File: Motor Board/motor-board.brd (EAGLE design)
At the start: 60 x 22 mm, 11 parts

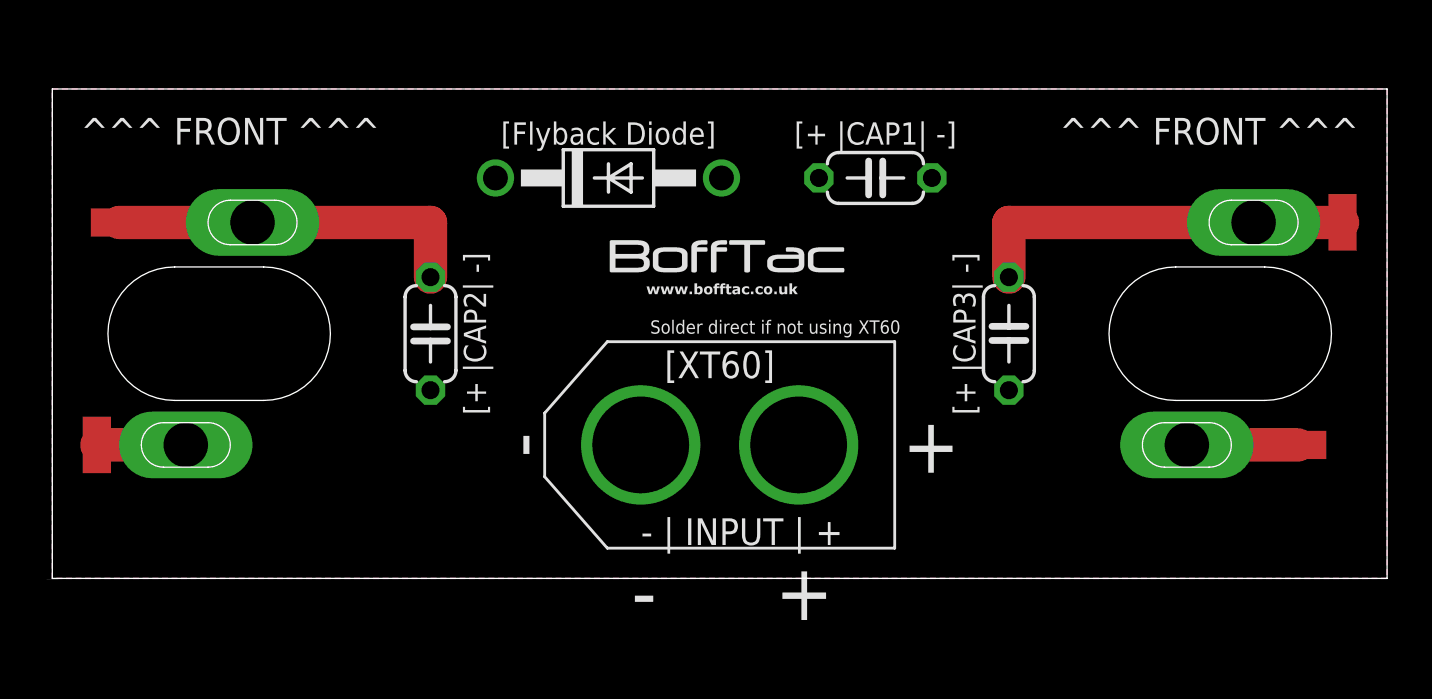
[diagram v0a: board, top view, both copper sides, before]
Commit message: Board Update
Redefined 130 motor can and updated board to add solder pads if not using XT60 connectors
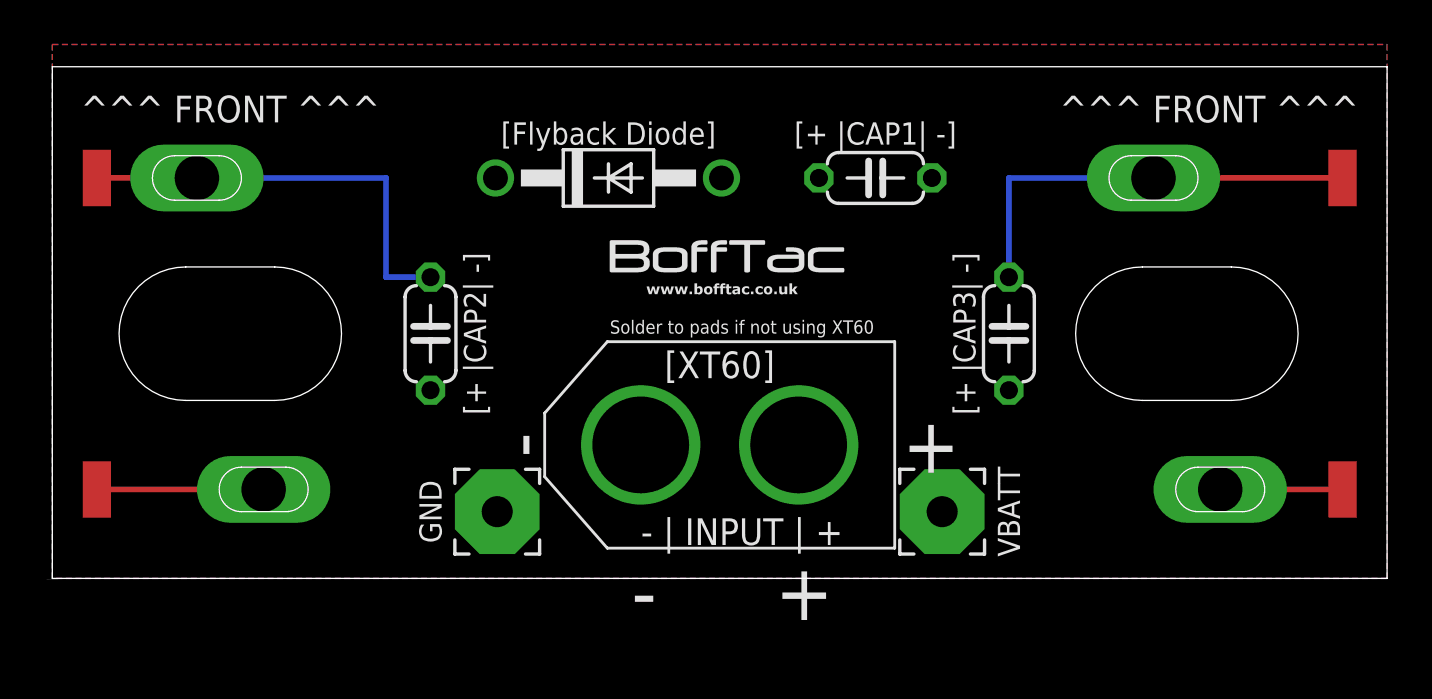
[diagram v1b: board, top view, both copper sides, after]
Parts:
- removed BOTTOM-MOTOR, TOP-MOTOR: (no value), 130-can:130-MOTOR-CAN
- removed PAD2, PAD3: (no value), wirepad:SMD1,27-2,54
- added BOTTOM-CAN, TOP-CAN: (no value), wirepad:SMD1,27-2,54
- added PAD-GND, PAD-VBATT: (no value), wirepad:3,81/1,4
- added U$1, U$2: 130-CAN-DEVICE130-MOTOR-CAN, 130-can:130-MOTOR-CAN
- moved PAD1 12.0 mm to (2.00, 18.0)
- moved PAD4 2.00 mm to (58.0, 18.0)
- turned C3 to 90 degrees
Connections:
- net GND: now also C1.2, C3.2, PAD-GND.1, PAD1.1, U$1.MOTOR-VE, U$2.MOTOR-VE; no longer BOTTOM-MOTOR.MOTOR-VE, C1.1, C3.1, PAD2.1, TOP-MOTOR.MOTOR-VE
- net VBATT: now also BOTTOM-CAN.1, C1.1, C3.1, PAD-VBATT.1, TOP-CAN.1, U$1.MOTOR+VE, U$2.MOTOR+VE; no longer BOTTOM-MOTOR.MOTOR+VE, C1.2, C3.2, PAD1.1, PAD3.1, TOP-MOTOR.MOTOR+VE
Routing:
- net GND: track 33.9 -> 38.9 mm
- net VBATT: track 9.00 -> 13.0 mm
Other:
- board size 60 x 22 mm -> 60 x 23 mm
- board text added: "GND"
- board text added: "Solder to pads if not using XT60"
- board text added: "VBATT"
- board text removed: "Solder direct if not using XT60"
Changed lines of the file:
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@@
 <plain>
 <wire x1="0" y1="0" x2="60" y2="0" width="0" layer="20"/>
-<wire x1="60" y1="0" x2="60" y2="22" width="0" layer="20"/>
-<wire x1="0" y1="22" x2="0" y2="0" width="0" layer="20"/>
-<wire x1="0" y1="22" x2="60" y2="22" width="0" layer="20"/>
+<wire x1="60" y1="0" x2="60" y2="23" width="0" layer="20"/>
+<wire x1="0" y1="23" x2="0" y2="0" width="0" layer="20"/>
+<wire x1="0" y1="23" x2="60" y2="23" width="0" layer="20"/>
 <text x="19" y="11" size="1" layer="25" ratio="12" rot="R90" align="center">[+ |CAP2| -]</text>
 <text x="25" y="19.5" size="1" layer="25" ratio="12" align="bottom-center">[Flyback Diode]</text>
 <text x="37" y="20" size="1" layer="25" ratio="12" rot="R180" align="center">[+ |CAP1| -]</text>
 <text x="41" y="11" size="1" layer="25" ratio="12" rot="R270" align="center">[+ |CAP3| -]</text>
-<text x="8" y="19.5" size="1.2" layer="25" ratio="12" align="bottom-center">^^^ FRONT ^^^</text>
-<text x="52" y="19.5" size="1.2" layer="25" ratio="12" align="bottom-center">^^^ FRONT ^^^</text>
+<text x="8" y="20.5" size="1.2" layer="25" ratio="12" align="bottom-center">^^^ FRONT ^^^</text>
+<text x="52" y="20.5" size="1.2" layer="25" ratio="12" align="bottom-center">^^^ FRONT ^^^</text>
 <text x="31" y="1.5" size="1.2" layer="25" ratio="12" align="bottom-center">- | INPUT | +</text>
-<text x="32.5" y="11" size="0.6" layer="25" ratio="12" align="bottom-center">Solder direct if not using XT60</text>
+<text x="31" y="11" size="0.6" layer="25" ratio="12" align="bottom-center">Solder to pads if not using XT60</text>
 <text x="30" y="9" size="1.2" layer="25" ratio="12" align="bottom-center">[XT60]</text>
 <text x="39.5" y="6" size="2.5" layer="25" ratio="12" align="center">+</text>
@@
 <rectangle x1="30.465" y1="15.195" x2="32.005" y2="15.205" layer="25"/>
 <text x="0" y="-0.05" size="0.02" layer="25" font="vector" ratio="12" align="bottom-center">Y:/BoffTac/Logo/monologo-w-address.bmp</text>
+<text x="17" y="3" size="1" layer="25" ratio="12" rot="R90" align="center">GND</text>
+<text x="43" y="3" size="1" layer="25" ratio="12" rot="R90" align="center">VBATT</text>
 </plain>
 <attributes>
@@
 <attribute name="VALUE" x="37.8675" y="10.94" size="1.27" layer="27" align="bottom-right"/>
 </element>
-<element name="TOP-MOTOR" library="130-can" package="130-MOTOR-CAN" value="" x="8" y="11" rot="R90"/>
-<element name="BOTTOM-MOTOR" library="130-can" package="130-MOTOR-CAN" value="" x="53" y="11" smashed="yes" rot="R90"/>
 <element name="C1" library="resistor" package="C050-024X044" value="" x="37" y="18" smashed="yes">
 <attribute name="VALUE" x="34.841" y="15.333" size="1.27" layer="27" ratio="10"/>
@@
 <attribute name="VALUE" x="45.667" y="8.841" size="1.27" layer="27" ratio="10" rot="R90"/>
 </element>
-<element name="C3" library="resistor" package="C050-024X044" value="" x="17" y="11" smashed="yes" rot="R270">
-<attribute name="VALUE" x="14.333" y="13.159" size="1.27" layer="27" ratio="10" rot="R270"/>
+<element name="C3" library="resistor" package="C050-024X044" value="" x="17" y="11" smashed="yes" rot="R90">
+<attribute name="VALUE" x="19.667" y="8.841" size="1.27" layer="27" ratio="10" rot="R90"/>
 </element>
-<element name="PAD1" library="wirepad" package="SMD1,27-2,54" value="" x="2" y="6" smashed="yes">
-<attribute name="VALUE" x="2" y="6" size="0.0254" layer="27"/>
+<element name="PAD1" library="wirepad" package="SMD1,27-2,54" value="" x="2" y="18" smashed="yes">
+<attribute name="VALUE" x="2" y="18" size="0.0254" layer="27"/>
 </element>
-<element name="PAD2" library="wirepad" package="SMD1,27-2,54" value="" x="3" y="16" smashed="yes" rot="R270">
-<attribute name="VALUE" x="3" y="16" size="0.0254" layer="27" rot="R270"/>
+<element name="TOP-CAN" library="wirepad" package="SMD1,27-2,54" value="" x="2" y="4" smashed="yes">
+<attribute name="VALUE" x="2" y="4" size="0.0254" layer="27"/>
 </element>
-<element name="PAD3" library="wirepad" package="SMD1,27-2,54" value="" x="56" y="6" smashed="yes" rot="R90">
-<attribute name="VALUE" x="56" y="6" size="0.0254" layer="27" rot="R90"/>
+<element name="BOTTOM-CAN" library="wirepad" package="SMD1,27-2,54" value="" x="58" y="4" smashed="yes" rot="R180">
+<attribute name="VALUE" x="58" y="4" size="0.0254" layer="27" rot="R180"/>
 </element>
-<element name="PAD4" library="wirepad" package="SMD1,27-2,54" value="" x="58" y="16" smashed="yes" rot="R180">
-<attribute name="VALUE" x="58" y="16" size="0.0254" layer="27" rot="R180"/>
+<element name="PAD4" library="wirepad" package="SMD1,27-2,54" value="" x="58" y="18" smashed="yes" rot="R180">
+<attribute name="VALUE" x="58" y="18" size="0.0254" layer="27" rot="R180"/>
+</element>
+<element name="U$1" library="130-can" package="130-MOTOR-CAN" value="130-CAN-DEVICE130-MOTOR-CAN" x="7.5" y="11" rot="MR90"/>
+<element name="U$2" library="130-can" package="130-MOTOR-CAN" value="130-CAN-DEVICE130-MOTOR-CAN" x="50.5" y="11" rot="MR90"/>
+<element name="PAD-GND" library="wirepad" package="3,81/1,4" value="" x="20" y="3" smashed="yes">
+<attribute name="VALUE" x="20" y="4.2" size="0.0254" layer="27"/>
+</element>
+<element name="PAD-VBATT" library="wirepad" package="3,81/1,4" value="" x="40" y="3" smashed="yes">
+<attribute name="VALUE" x="40" y="4.2" size="0.0254" layer="27"/>
 </element>
 </elements>
@@
 <signal name="GND">
 <polygon width="0.254" layer="16" isolate="0.3048">
-<vertex x="0" y="22"/>
-<vertex x="60" y="22"/>
+<vertex x="0" y="24"/>
+<vertex x="60" y="24"/>
 <vertex x="60" y="0"/>
 <vertex x="0" y="0"/>
 </polygon>
-<contactref element="TOP-MOTOR" pad="MOTOR-VE"/>
-<contactref element="BOTTOM-MOTOR" pad="MOTOR-VE"/>
+<contactref element="U$2" pad="MOTOR-VE"/>
 <contactref element="J1" pad="-"/>
+<contactref element="U$1" pad="MOTOR-VE"/>
+<contactref element="C1" pad="2"/>
+<contactref element="C2" pad="2"/>
+<contactref element="C3" pad="2"/>
+<contactref element="PAD4" pad="1"/>
+<contactref element="PAD1" pad="1"/>
+<wire x1="49.5" y1="18" x2="43" y2="18" width="0.254" layer="16"/>
+<wire x1="43" y1="18" x2="43" y2="13.54" width="0.254" layer="16"/>
+<wire x1="58" y1="18" x2="49.5" y2="18" width="0.254" layer="1"/>
+<wire x1="17" y1="13.54" x2="15" y2="13.54" width="0.254" layer="16"/>
+<wire x1="15" y1="13.54" x2="15" y2="18" width="0.254" layer="16"/>
+<wire x1="15" y1="18" x2="6.5" y2="18" width="0.254" layer="16"/>
 <contactref element="D1" pad="A"/>
-<contactref element="C1" pad="1"/>
-<contactref element="C2" pad="2"/>
-<contactref element="C3" pad="1"/>
-<contactref element="PAD2" pad="1"/>
-<contactref element="PAD4" pad="1"/>
-<wire x1="54" y1="16" x2="43" y2="16" width="1.5" layer="1"/>
-<wire x1="43" y1="16" x2="43" y2="13.54" width="1.5" layer="1"/>
-<wire x1="58" y1="16" x2="54" y2="16" width="1.5" layer="1"/>
-<wire x1="3" y1="16" x2="9" y2="16" width="1.5" layer="1"/>
-<wire x1="17" y1="13.54" x2="17" y2="16" width="1.5" layer="1"/>
-<wire x1="17" y1="16" x2="9" y2="16" width="1.5" layer="1"/>
+<wire x1="2" y1="18" x2="6.5" y2="18" width="0.254" layer="1"/>
+<contactref element="PAD-GND" pad="1"/>
 </signal>
 <signal name="VBATT">
 <polygon width="0.254" layer="1" isolate="0.3048">
-<vertex x="0" y="22"/>
-<vertex x="60" y="22"/>
+<vertex x="0" y="24"/>
+<vertex x="60" y="24"/>
 <vertex x="60" y="0"/>
 <vertex x="0" y="0"/>
 </polygon>
-<contactref element="BOTTOM-MOTOR" pad="MOTOR+VE"/>
-<contactref element="TOP-MOTOR" pad="MOTOR+VE"/>
 <contactref element="J1" pad="+"/>
+<contactref element="U$1" pad="MOTOR+VE"/>
+<contactref element="U$2" pad="MOTOR+VE"/>
+<contactref element="C1" pad="1"/>
+<contactref element="C2" pad="1"/>
+<contactref element="C3" pad="1"/>
+<contactref element="BOTTOM-CAN" pad="1"/>
+<contactref element="TOP-CAN" pad="1"/>
+<wire x1="2" y1="4" x2="9.5" y2="4" width="0.254" layer="1"/>
+<wire x1="58" y1="4" x2="52.5" y2="4" width="0.254" layer="1"/>
 <contactref element="D1" pad="C"/>
-<contactref element="C1" pad="2"/>
-<contactref element="C2" pad="1"/>
-<contactref element="C3" pad="2"/>
-<contactref element="PAD3" pad="1"/>
-<contactref element="PAD1" pad="1"/>
-<wire x1="56" y1="6" x2="51" y2="6" width="1.5" layer="1"/>
-<wire x1="2" y1="6" x2="6" y2="6" width="1.5" layer="1"/>
+<contactref element="PAD-VBATT" pad="1"/>
 </signal>
 </signals>
